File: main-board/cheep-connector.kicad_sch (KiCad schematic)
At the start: 5 parts, among them J1 Conn_02x16_Odd_Even, J2 Conn_02x16_Odd_Even, J3 Conn_02x16_Odd_Even, J4 Conn_02x16_Odd_Even, J5 Conn_02x10_Odd_Even

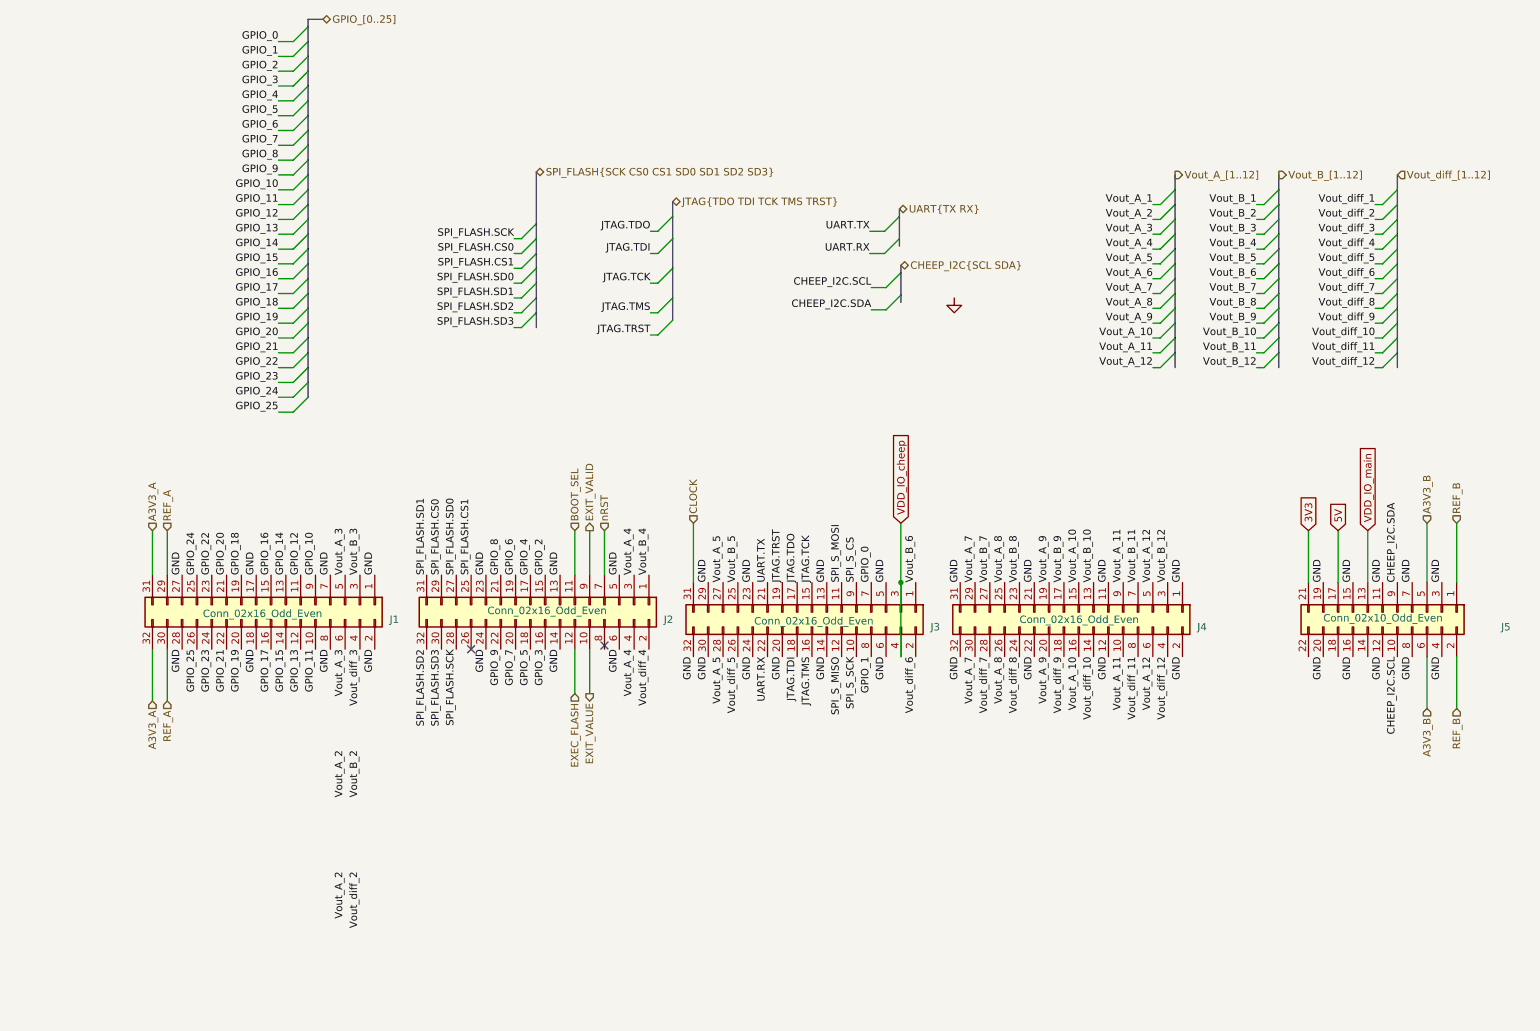
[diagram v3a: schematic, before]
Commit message: Connector bugfixing, added new connector to layout
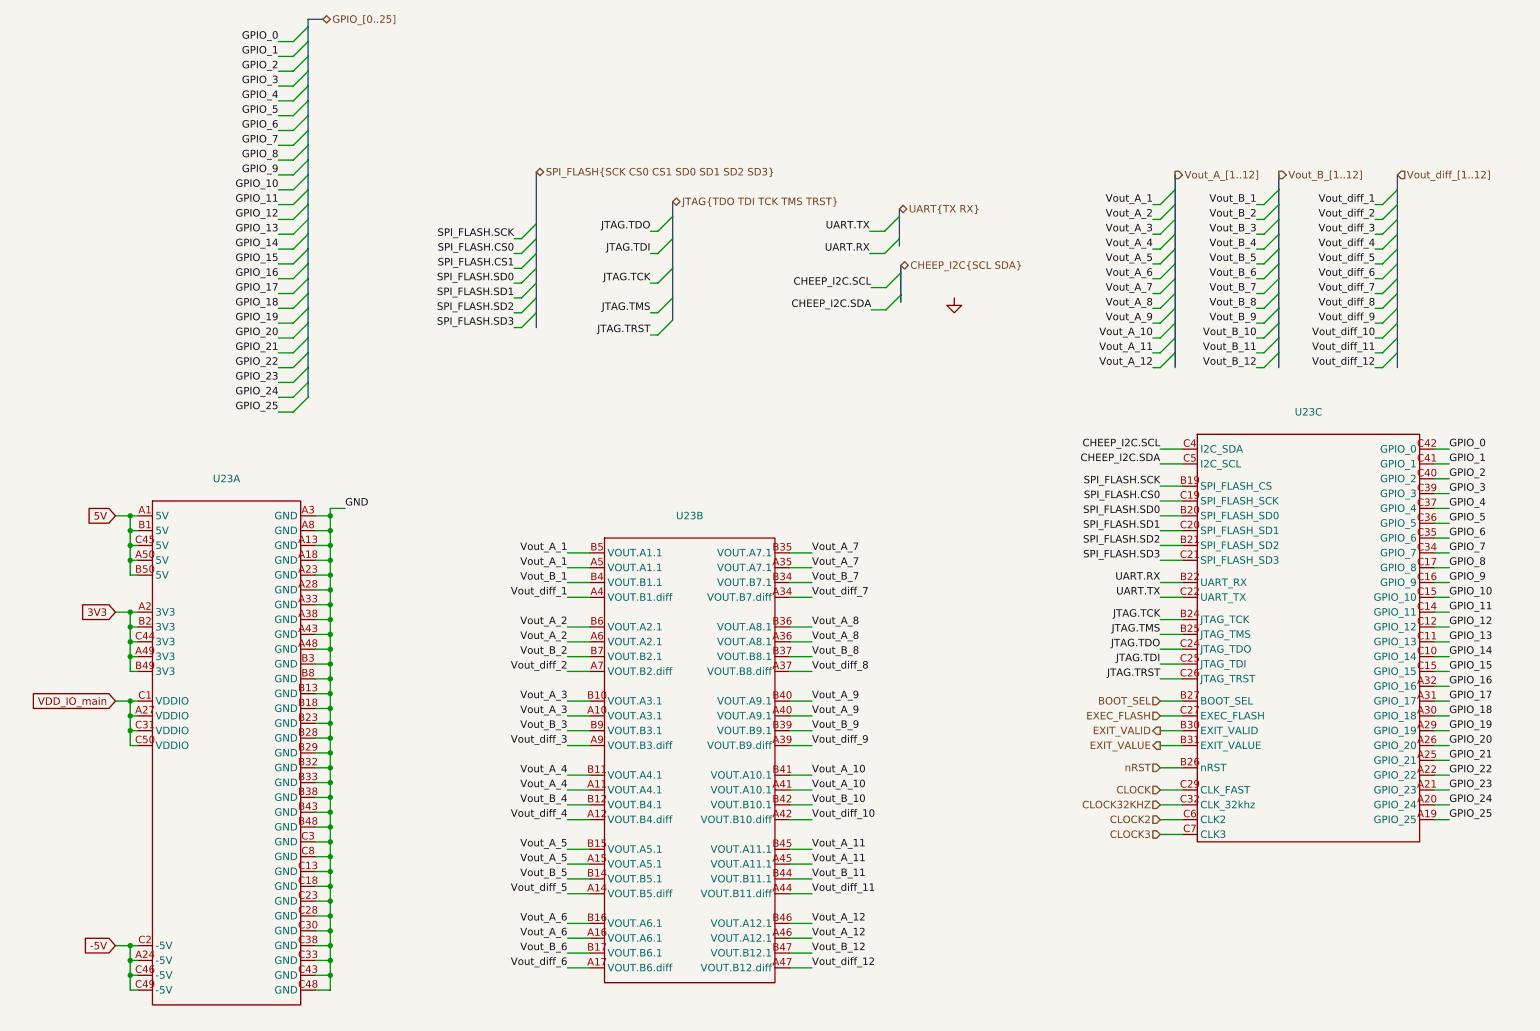
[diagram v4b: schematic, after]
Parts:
- removed J1, J2, J3, J4: Conn_02x16_Odd_Even, symbol Connector_Generic:Conn_02x16_Odd_Even
- removed J5: Conn_02x10_Odd_Even, symbol Connector_Generic:Conn_02x11_Odd_Even
- added U23: ~, heep_footprints:CHEEP_CONNECTOR_MAINBOARD, symbol cheeps-tb:CheepConnectorFull
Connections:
- net 3V3: now also U23.A2 (3V3), U23.A49 (3V3), U23.B2 (3V3), U23.B49 (3V3), U23.C44 (3V3)
- net 5V: now also U23.A1 (5V), U23.A50 (5V), U23.B1 (5V), U23.B50 (5V), U23.C45 (5V)
- net BOOT_SEL: now also U23.B27 (BOOT_SEL)
- net CHEEP_I2C.SCL: now also U23.C4 (I2C_SDA)
- net CHEEP_I2C.SDA: now also U23.C5 (I2C_SCL)
- net CLOCK: now also U23.C29 (CLK_FAST)
- net EXEC_FLASH: now also U23.C27 (EXEC_FLASH)
- net EXIT_VALID: now also U23.B30 (EXIT_VALID)
- net EXIT_VALUE: now also U23.B31 (EXIT_VALUE)
- net GND: now also U23.A13 (GND), U23.A18 (GND), U23.A23 (GND), U23.A28 (GND), U23.A3 (GND), U23.A33 (GND), U23.A38 (GND), U23.A43 (GND), U23.A48 (GND), U23.A8 (GND), U23.B13 (GND), U23.B18 (GND), U23.B23 (GND), U23.B28 (GND), U23.B29 (GND), U23.B3 (GND), U23.B32 (GND), U23.B33 (GND), U23.B38 (GND), U23.B43 (GND), U23.B48 (GND), U23.B8 (GND), U23.C13 (GND), U23.C18 (GND), U23.C23 (GND), U23.C28 (GND), U23.C3 (GND), U23.C30 (GND), U23.C33 (GND), U23.C38 (GND), U23.C43 (GND), U23.C48 (GND), U23.C8 (GND)
- net GPIO_0: now also U23.C42 (GPIO_0)
- net GPIO_1: now also U23.C41 (GPIO_1)
- net GPIO_10: now also U23.C15 (GPIO_15)
- net GPIO_11: now also U23.C14 (GPIO_11)
- net GPIO_12: now also U23.C12 (GPIO_12)
- net GPIO_13: now also U23.C11 (GPIO_13)
- net GPIO_14: now also U23.C10 (GPIO_14)
- net GPIO_15: now also U23.C15 (GPIO_15)
- net GPIO_16: now also U23.A32 (GPIO_16)
- net GPIO_17: now also U23.A31 (GPIO_17)
- net GPIO_18: now also U23.A30 (GPIO_18)
- net GPIO_19: now also U23.A29 (GPIO_19)
- net GPIO_2: now also U23.C40 (GPIO_2)
- net GPIO_20: now also U23.A26 (GPIO_20)
- net GPIO_21: now also U23.A25 (GPIO_21)
- net GPIO_22: now also U23.A22 (GPIO_22)
- net GPIO_23: now also U23.A21 (GPIO_23)
- net GPIO_24: now also U23.A20 (GPIO_24)
- net GPIO_25: now also U23.A19 (GPIO_25)
- net GPIO_3: now also U23.C39 (GPIO_3)
- net GPIO_4: now also U23.C37 (GPIO_4)
- net GPIO_5: now also U23.C36 (GPIO_5)
- net GPIO_6: now also U23.C35 (GPIO_6)
- net GPIO_7: now also U23.C34 (GPIO_7)
- net GPIO_8: now also U23.C17 (GPIO_8)
- net GPIO_9: now also U23.C16 (GPIO_9)
- net JTAG.TCK: now also U23.B24 (JTAG_TCK)
- net JTAG.TDI: now also U23.C25 (JTAG_TDI)
- net JTAG.TDO: now also U23.C24 (JTAG_TDO)
- net JTAG.TMS: now also U23.B25 (JTAG_TMS)
- net JTAG.TRST: now also U23.C26 (JTAG_TRST)
- net SPI_FLASH.CS0: now also U23.C19 (SPI_FLASH_SCK)
- net SPI_FLASH.SCK: now also U23.B19 (SPI_FLASH_CS)
- net SPI_FLASH.SD0: now also U23.B20 (SPI_FLASH_SD0)
- net SPI_FLASH.SD1: now also U23.C20 (SPI_FLASH_SD1)
- net SPI_FLASH.SD2: now also U23.B21 (SPI_FLASH_SD2)
- net SPI_FLASH.SD3: now also U23.C21 (SPI_FLASH_SD3)
- net UART.RX: now also U23.B22 (UART_RX)
- net UART.TX: now also U23.C22 (UART_TX)
- net VDD_IO_main: now also U23.A27 (VDDIO), U23.C1 (VDDIO), U23.C31 (VDDIO), U23.C50 (VDDIO)
- net Vout_A_1: now also U23.A5 (VOUT.A1.1), U23.B5 (VOUT.A1.1)
- net Vout_A_10: now also U23.A41 (VOUT.A10.1), U23.B41 (VOUT.A10.1)
- net Vout_A_11: now also U23.A45 (VOUT.A11.1), U23.B45 (VOUT.A11.1)
- net Vout_A_12: now also U23.A46 (VOUT.A12.1), U23.B46 (VOUT.A12.1)
- net Vout_A_2: now also U23.A6 (VOUT.A2.1), U23.B6 (VOUT.A2.1)
- net Vout_A_3: now also U23.A10 (VOUT.A3.1), U23.B10 (VOUT.A3.1)
- net Vout_A_4: now also U23.A11 (VOUT.A4.1), U23.B11 (VOUT.A4.1)
- net Vout_A_5: now also U23.A15 (VOUT.A5.1), U23.B15 (VOUT.A5.1)
- net Vout_A_6: now also U23.A16 (VOUT.A6.1), U23.B16 (VOUT.A6.1)
- net Vout_A_7: now also U23.A35 (VOUT.A7.1), U23.B35 (VOUT.A7.1)
- net Vout_A_8: now also U23.A36 (VOUT.A8.1), U23.B36 (VOUT.A8.1)
- net Vout_A_9: now also U23.A40 (VOUT.A9.1), U23.B40 (VOUT.A9.1)
- net Vout_B_1: now also U23.B4 (VOUT.B1.1)
- net Vout_B_10: now also U23.B42 (VOUT.B10.1)
- net Vout_B_11: now also U23.B44 (VOUT.B11.1)
- net Vout_B_12: now also U23.B47 (VOUT.B12.1)
- net Vout_B_2: now also U23.B7 (VOUT.B2.1)
- net Vout_B_3: now also U23.B9 (VOUT.B3.1)
- net Vout_B_4: now also U23.B12 (VOUT.B4.1)
- net Vout_B_5: now also U23.B14 (VOUT.B5.1)
- net Vout_B_6: now also U23.B17 (VOUT.B6.1)
- net Vout_B_7: now also U23.B34 (VOUT.B7.1)
- net Vout_B_8: now also U23.B37 (VOUT.B8.1)
- net Vout_B_9: now also U23.B39 (VOUT.B9.1)
- net Vout_diff_1: now also U23.A4 (VOUT.B1.diff)
- net Vout_diff_10: now also U23.A42 (VOUT.B10.diff)
- net Vout_diff_11: now also U23.A44 (VOUT.B11.diff)
- net Vout_diff_12: now also U23.A47 (VOUT.B12.diff)
- net Vout_diff_2: now also U23.A7 (VOUT.B2.diff)
- net Vout_diff_3: now also U23.A9 (VOUT.B3.diff)
- net Vout_diff_4: now also U23.A12 (VOUT.B4.diff)
- net Vout_diff_5: now also U23.A14 (VOUT.B5.diff)
- net Vout_diff_6: now also U23.A17 (VOUT.B6.diff)
- net Vout_diff_7: now also U23.A34 (VOUT.B7.diff)
- net Vout_diff_8: now also U23.A37 (VOUT.B8.diff)
- net Vout_diff_9: now also U23.A39 (VOUT.B9.diff)
- net nRST: now also U23.B26 (nRST)
- new net -5V: U23.A24 (-5V), U23.C2 (-5V), U23.C46 (-5V), U23.C49 (-5V)
- new net CLOCK2: U23.C6 (CLK2)
- new net CLOCK3: U23.C7 (CLK3)
- new net CLOCK32KHZ: U23.C32 (CLK_32khz)
- no-connect marks 2 -> 0

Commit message: update testing board
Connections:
- net VDD_IO_main renamed VDDIO
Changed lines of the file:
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@@
 		)
 	)
-	(global_label "VDD_IO_main"
+	(global_label "VDDIO"
 		(shape input)
 		(at 30.48 139.7 180)
@@
 		)
 		(property "Intersheetrefs" "${INTERSHEET_REFS}"
-			(at 15.3996 139.7 0)
+			(at 21.9309 139.7 0)
 			(effects
 				(font

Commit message: pcb update
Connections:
- net GPIO_15: now also U23.C9 (GPIO_15); no longer U23.C15 (GPIO_15)
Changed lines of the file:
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@@
 		(pin "A43"
 		)
-		(pin "A48"
+		(pin "A49"
 		)
 		(pin "B3"
@@
 		(pin "B43"
 		)
-		(pin "B48"
+		(pin "B49"
 		)
 		(pin "C3"
@@
 		(pin "C10"
 		)
-		(pin "C15"
+		(pin "C9"
 		)
 		(pin "A32"

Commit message: PCB update
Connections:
- net -5V: now also U23.A22 (-5V); no longer U23.A24 (-5V)
- net CLOCK2: now also U23.A26 (CLK2); no longer U23.C6 (CLK2)
- net CLOCK3: now also U23.A25 (CLK3); no longer U23.C7 (CLK3)
- net GND: now also U23.A24 (GND)
- net GPIO_20: now also U23.A21 (GPIO_20); no longer U23.A26 (GPIO_20)
- net GPIO_21: now also U23.A20 (GPIO_21); no longer U23.A25 (GPIO_21)
- net GPIO_22: now also U23.A19 (GPIO_22); no longer U23.A22 (GPIO_22)
- net GPIO_23: no longer U23.A21 (GPIO_23)
- net GPIO_24: no longer U23.A20 (GPIO_24)
- net GPIO_25: no longer U23.A19 (GPIO_25)
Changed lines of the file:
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@@
 	)
 	(junction
+		(at 67.31 189.23)
+		(diameter 0)
+		(color 0 0 0 0)
+	)
+	(junction
 		(at 67.31 148.59)
 		(diameter 0)
@@
 	(wire
 		(pts
+			(xy 64.77 191.77) (xy 67.31 191.77)
+		)
+		(stroke
+			(width 0)
+			(type default)
+		)
+	)
+	(wire
+		(pts
 			(xy 64.77 113.03) (xy 67.31 113.03)
 		)
@@
 		)
 	)
-	(wire
-		(pts
-			(xy 259.08 160.02) (xy 256.54 160.02)
-		)
-		(stroke
-			(width 0)
-			(type default)
-		)
-	)
 	(bus
 		(pts
@@
 	(wire
 		(pts
-			(xy 259.08 154.94) (xy 256.54 154.94)
-		)
-		(stroke
-			(width 0)
-			(type default)
-		)
-	)
-	(wire
-		(pts
 			(xy 149.86 177.8) (xy 146.05 177.8)
 		)
@@
 	(wire
 		(pts
-			(xy 259.08 157.48) (xy 256.54 157.48)
+			(xy 149.86 139.7) (xy 146.05 139.7)
 		)
 		(stroke
@@
 	(wire
 		(pts
-			(xy 149.86 139.7) (xy 146.05 139.7)
+			(xy 64.77 168.91) (xy 67.31 168.91)
 		)
 		(stroke
@@
 	(wire
 		(pts
-			(xy 64.77 168.91) (xy 67.31 168.91)
+			(xy 208.28 80.01) (xy 209.55 80.01)
 		)
 		(stroke
@@
 	(wire
 		(pts
-			(xy 208.28 80.01) (xy 209.55 80.01)
+			(xy 107.95 147.32) (xy 111.76 147.32)
 		)
 		(stroke
@@
 	(wire
 		(pts
-			(xy 107.95 147.32) (xy 111.76 147.32)
+			(xy 67.31 191.77) (xy 67.31 189.23)
 		)
 		(stroke
@@
 		)
 	)
-	(label "GPIO_23"
-		(at 259.08 154.94 0)
-		(effects
-			(font
-				(size 1.27 1.27)
-			)
-			(justify left bottom)
-		)
-	)
 	(label "SPI_FLASH.CS0"
 		(at 98.806 62.992 180)
@@
 		)
 	)
-	(label "GPIO_25"
-		(at 259.08 160.02 0)
-		(effects
-			(font
-				(size 1.27 1.27)
-			)
-			(justify left bottom)
-		)
-	)
 	(label "GPIO_11"
 		(at 259.08 124.46 0)
@@
 		)
 	)
-	(label "GPIO_24"
-		(at 259.08 157.48 0)
-		(effects
-			(font
-				(size 1.27 1.27)
-			)
-			(justify left bottom)
-		)
-	)
 	(label "Vout_diff_8"
 		(at 149.86 134.62 0)
@@
 		(pin "C45"
 		)
-		(pin "C6"
-		)
-		(pin "C7"
-		)
 		(instances
 			(project ""
@@
 		(pin "C10"
 		)
-		(pin "C15"
+		(pin "C9"
 		)
 		(pin "A32"
@@
 		(pin "C45"
 		)
-		(pin "C6"
-		)
-		(pin "C7"
-		)
 		(instances
